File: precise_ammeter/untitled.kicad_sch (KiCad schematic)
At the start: 16 parts, among them U1 INA121U, U2 TLV9301xDBV

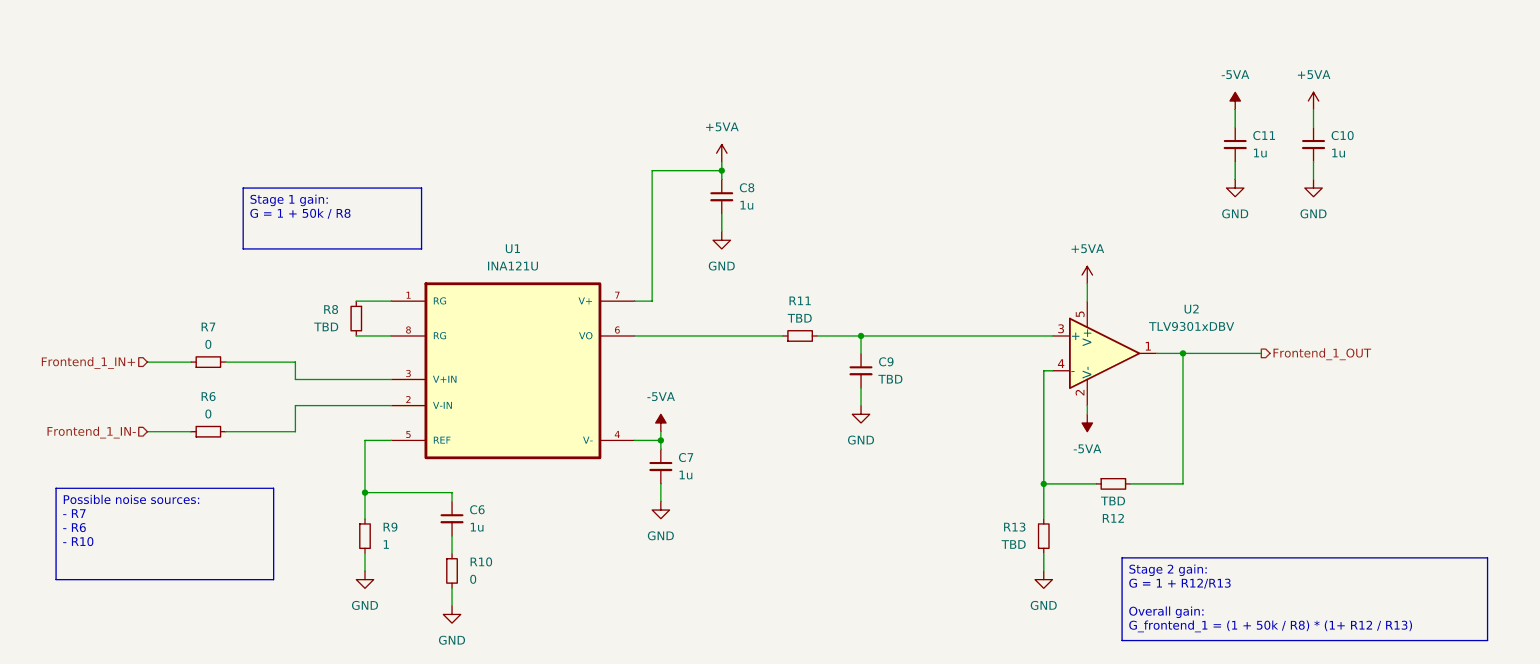
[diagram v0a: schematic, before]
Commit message: Dodano drugi schemat frontendu
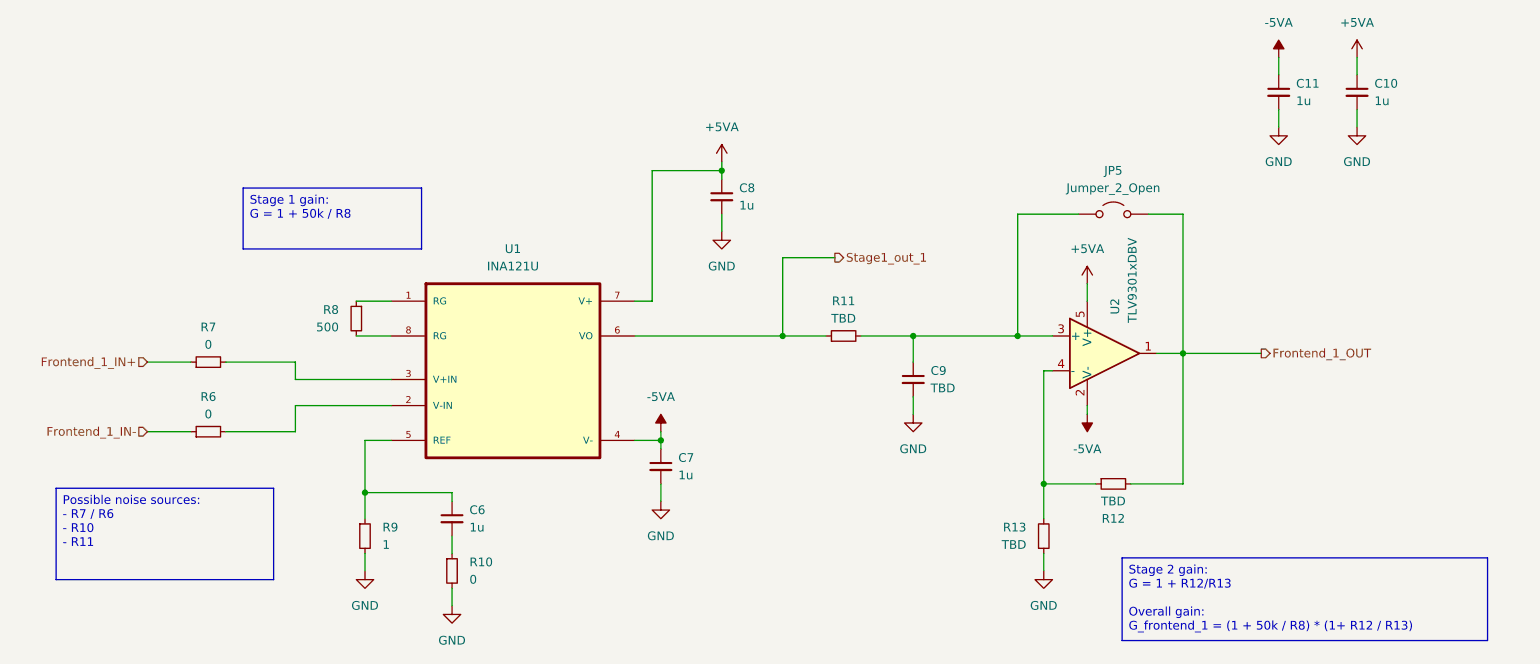
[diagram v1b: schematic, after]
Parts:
- added JP5: Jumper_2_Open, symbol Jumper:Jumper_2_Open
- R8: value TBD -> 500
- U1: footprint INA121U:SOIC127P599X175-8N -> Package_DIP:DIP-8_W7.62mm_LongPads
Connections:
- net Frontend_1_OUT: now also JP5.2 (B)
- net at C9.1, R11.2, U2.3 (+): now also JP5.1 (A)
- net Stage1_out_1: now reaches R11.1, U1.6 (VO)
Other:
- moved on the sheet: C10, C11, C9, R11

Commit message: dodano layout
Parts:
- JP5: footprint (none) -> Jumper:SolderJumper-2_P1.3mm_Open_Pad1.0x1.5mm
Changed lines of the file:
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@@
 			)
 		)
-		(property "Footprint" ""
+		(property "Footprint" "Jumper:SolderJumper-2_P1.3mm_Open_Pad1.0x1.5mm"
 			(at 199.39 71.12 0)
 			(effects

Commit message: dodano warrtosci elementow w frontend1
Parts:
- C6: value 1u -> DNP
- C9: value TBD -> 1u
- R10: value 0 -> DNP
- R11: value TBD -> 22k
- R12: value TBD -> 150k
- R13: value TBD -> 10k
- R6, R7: value 0 -> 22k
- R8: value 500 -> 1k
- R9: value 1 -> 0
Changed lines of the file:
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@@
 			)
 		)
-		(property "Value" "1"
+		(property "Value" "0"
 			(at 92.71 119.3799 0)
 			(effects
@@
 			)
 		)
-		(property "Value" "TBD"
+		(property "Value" "1u"
 			(at 172.72 96.5262 0)
 			(effects
@@
 			)
 		)
-		(property "Value" "0"
+		(property "Value" "22k"
 			(at 67.31 100.33 90)
 			(effects
@@
 			)
 		)
-		(property "Value" "TBD"
+		(property "Value" "10k"
 			(at 186.69 119.3799 0)
 			(effects
@@
 			)
 		)
-		(property "Value" "500"
+		(property "Value" "1k"
 			(at 86.36 87.6299 0)
 			(effects
@@
 			)
 		)
-		(property "Value" "TBD"
+		(property "Value" "150k"
 			(at 199.39 113.03 90)
 			(effects
@@
 			)
 		)
-		(property "Value" "0"
+		(property "Value" "DNP"
 			(at 105.41 124.4599 0)
 			(effects
@@
 			)
 		)
-		(property "Value" "1u"
+		(property "Value" "DNP"
 			(at 105.41 116.8462 0)
 			(effects
@@
 			)
 		)
-		(property "Value" "TBD"
+		(property "Value" "22k"
 			(at 160.02 86.36 90)
 			(effects
@@
 			)
 		)
-		(property "Value" "0"
+		(property "Value" "22k"
 			(at 67.31 90.17 90)
 			(effects

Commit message: unknown changes
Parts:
- R8: value 1k -> 1.2k
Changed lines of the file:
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@@
 			)
 		)
-		(property "Value" "1k"
+		(property "Value" "1.2k"
 			(at 86.36 87.6299 0)
 			(effects
